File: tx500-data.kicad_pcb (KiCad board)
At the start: 2 copper layers, 50 x 79 mm, 51 parts, among them J1 USB_B_Micro, J2 CAT, J3 REM/DATA, J4 USB_A, U1 TUSB2036, U2 FT232RL, U3 HS-100B, U4 TPS76333, U5 TPS2044D, U6 SN75240, U7 SN75240, Y1 6MHz

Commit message: Add 3D models, and various cleanup
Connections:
- J1 pad 4: (no net) -> Net-(J1-Pad4)
- U1 pad 21: (no net) -> Net-(U1-Pad21)
- U1 pad 32: (no net) -> Net-(U1-Pad32)
- U1 pad 4: (no net) -> Net-(U1-Pad4)
- U1 pad 5: (no net) -> Net-(U1-Pad5)
- U2 pad 10: (no net) -> Net-(U2-Pad10)
- U2 pad 11: (no net) -> Net-(U2-Pad11)
- U2 pad 12: (no net) -> Net-(U2-Pad12)
- U2 pad 13: (no net) -> Net-(U2-Pad13)
- U2 pad 19: (no net) -> Net-(U2-Pad19)
- U2 pad 2: (no net) -> Net-(U2-Pad2)
- U2 pad 22: (no net) -> Net-(U2-Pad22)
- U2 pad 23: (no net) -> Net-(U2-Pad23)
- U2 pad 27: (no net) -> Net-(U2-Pad27)
- U2 pad 28: (no net) -> Net-(U2-Pad28)
- U2 pad 3: (no net) -> Net-(U2-Pad3)
- U2 pad 6: (no net) -> Net-(U2-Pad6)
- U2 pad 9: (no net) -> Net-(U2-Pad9)
- U3 pad 1: (no net) -> Net-(U3-Pad1)
- U3 pad 11: (no net) -> Net-(U3-Pad11)
- U3 pad 17: (no net) -> Net-(U3-Pad17)
- U3 pad 19: (no net) -> Net-(U3-Pad19)
- U3 pad 2: (no net) -> Net-(U3-Pad2)
- U3 pad 26: (no net) -> Net-(U3-Pad26)
- U3 pad 27: (no net) -> Net-(U3-Pad27)
- U3 pad 3: (no net) -> Net-(U3-Pad3)
- U3 pad 31: (no net) -> Net-(U3-Pad31)
- U3 pad 39: (no net) -> Net-(U3-Pad39)
- U3 pad 4: (no net) -> Net-(U3-Pad4)
- U3 pad 41: (no net) -> Net-(U3-Pad41)
- U3 pad 42: (no net) -> Net-(U3-Pad42)
- U3 pad 47: (no net) -> Net-(U3-Pad47)
- U3 pad 5: (no net) -> Net-(U3-Pad5)
- U3 pad 7: (no net) -> Net-(U3-Pad7)
- U4 pad 4: (no net) -> Net-(U4-Pad4)
- U5 pad 10: (no net) -> Net-(U5-Pad10)
- U5 pad 9: (no net) -> Net-(U5-Pad9)
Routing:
- net GNDREF: track 155.4 -> 175.9 mm
- net +3V3: track 57.7 -> 58.6 mm

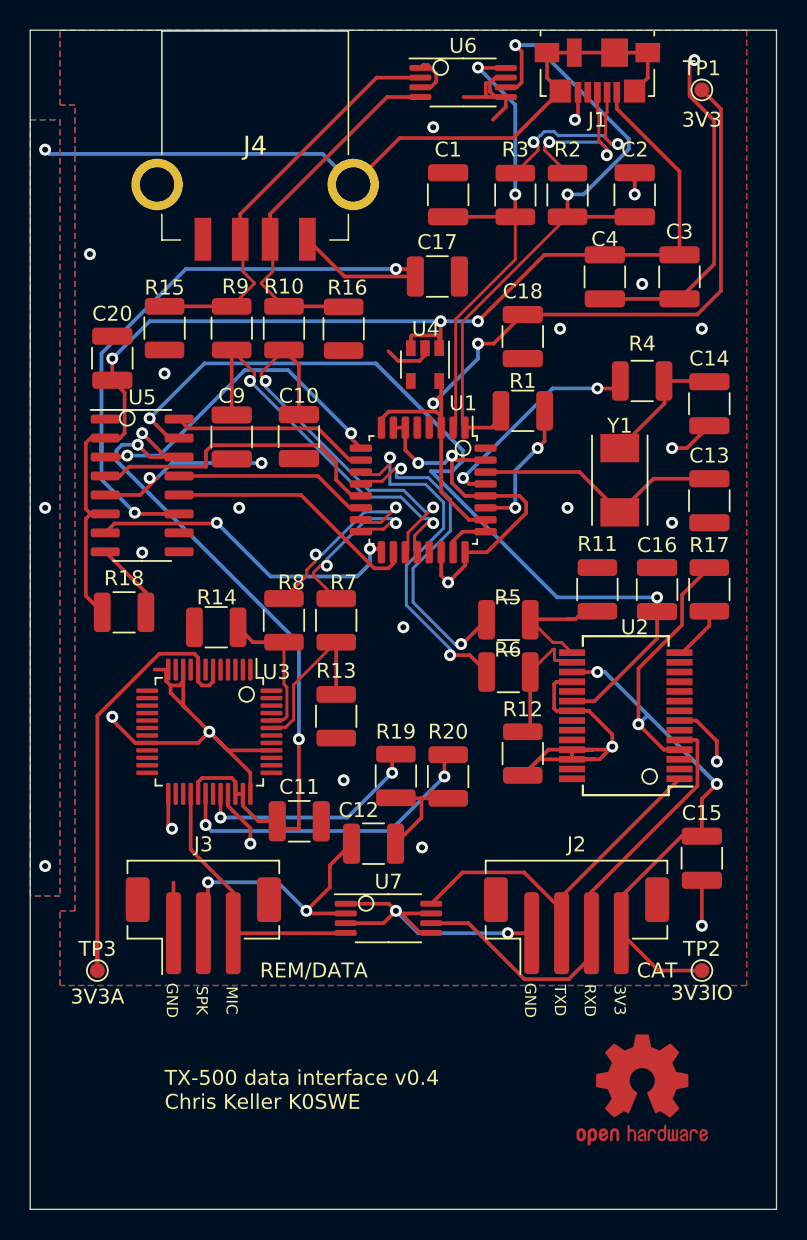
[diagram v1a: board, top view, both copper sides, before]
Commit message: Fix crystal BOM and footprint
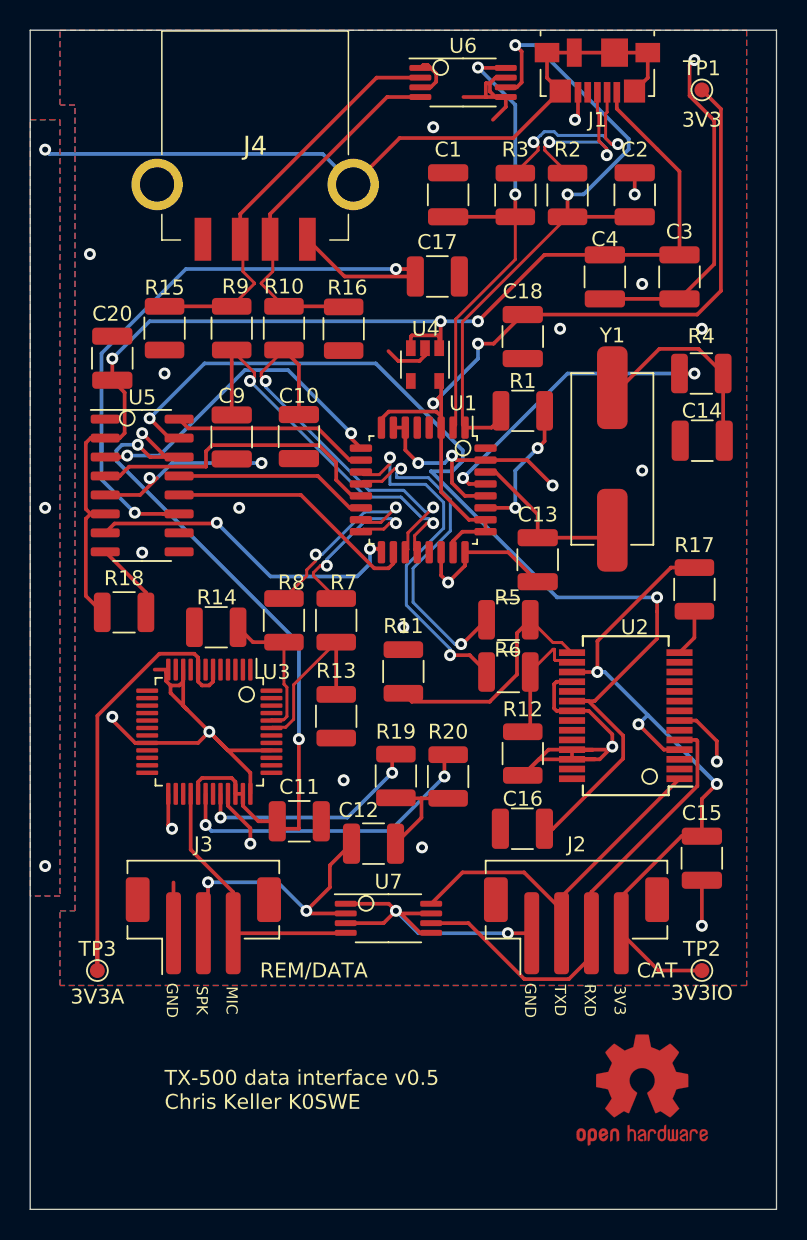
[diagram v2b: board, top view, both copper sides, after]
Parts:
- Y1: footprint Crystal:Crystal_SMD_Abracon_ABM7-2Pin_6.0x3.5mm -> XT49M:XT49M
- moved C16 18.4 mm to (162.0, 111.5), turned to 180 degrees
- moved R11 14.1 mm to (154.0, 101.0)
- moved C13 12.2 mm to (163.0, 93.5)
- moved R4 3.99 mm to (174.0, 81.0)
- moved C14 2.52 mm to (174.0, 85.5), turned to 180 degrees
- moved Y1 1.51 mm to (168.0, 86.7)
- moved R17 1.00 mm to (173.5, 95.5)
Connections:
- J1 pad 4: Net-(J1-Pad4) -> (no net)
- U1 pad 21: Net-(U1-Pad21) -> (no net)
- U1 pad 32: Net-(U1-Pad32) -> (no net)
- U1 pad 4: Net-(U1-Pad4) -> (no net)
- U1 pad 5: Net-(U1-Pad5) -> (no net)
- U2 pad 10: Net-(U2-Pad10) -> (no net)
- U2 pad 11: Net-(U2-Pad11) -> (no net)
- U2 pad 12: Net-(U2-Pad12) -> (no net)
- U2 pad 13: Net-(U2-Pad13) -> (no net)
- U2 pad 19: Net-(U2-Pad19) -> (no net)
- U2 pad 2: Net-(U2-Pad2) -> (no net)
- U2 pad 22: Net-(U2-Pad22) -> (no net)
- U2 pad 23: Net-(U2-Pad23) -> (no net)
- U2 pad 27: Net-(U2-Pad27) -> (no net)
- U2 pad 28: Net-(U2-Pad28) -> (no net)
- U2 pad 3: Net-(U2-Pad3) -> (no net)
- U2 pad 6: Net-(U2-Pad6) -> (no net)
- U2 pad 9: Net-(U2-Pad9) -> (no net)
- U3 pad 1: Net-(U3-Pad1) -> (no net)
- U3 pad 11: Net-(U3-Pad11) -> (no net)
- U3 pad 17: Net-(U3-Pad17) -> (no net)
- U3 pad 19: Net-(U3-Pad19) -> (no net)
- U3 pad 2: Net-(U3-Pad2) -> (no net)
- U3 pad 26: Net-(U3-Pad26) -> (no net)
- U3 pad 27: Net-(U3-Pad27) -> (no net)
- U3 pad 3: Net-(U3-Pad3) -> (no net)
- U3 pad 31: Net-(U3-Pad31) -> (no net)
- U3 pad 39: Net-(U3-Pad39) -> (no net)
- U3 pad 4: Net-(U3-Pad4) -> (no net)
- U3 pad 41: Net-(U3-Pad41) -> (no net)
- U3 pad 42: Net-(U3-Pad42) -> (no net)
- U3 pad 47: Net-(U3-Pad47) -> (no net)
- U3 pad 5: Net-(U3-Pad5) -> (no net)
- U3 pad 7: Net-(U3-Pad7) -> (no net)
- U4 pad 4: Net-(U4-Pad4) -> (no net)
- U5 pad 10: Net-(U5-Pad10) -> (no net)
- U5 pad 9: Net-(U5-Pad9) -> (no net)
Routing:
- net /5VA: track 59.4 -> 72.5 mm
- net Net-(R11-Pad1): track 8.88 -> 16.3 mm
- net Net-(C14-Pad1): track 7.69 -> 13.9 mm
- net /XTAL2: track 14.9 -> 21.1 mm
- net /XTAL1: track 17.0 -> 11.4 mm
- net /3V3IO: track 53.0 -> 51.2 mm
- net GNDREF: track 175.9 -> 174.9 mm, vias 31 -> 30
- net /PWREN: track 3.72 -> 3.19 mm
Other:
- board text added: "TX-500 data interface v0.5 Chris Keller K0SWE"
- board text removed: "TX-500 data interface v0.4 Chris Keller K0SWE"

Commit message: Use standard footprint for crystal
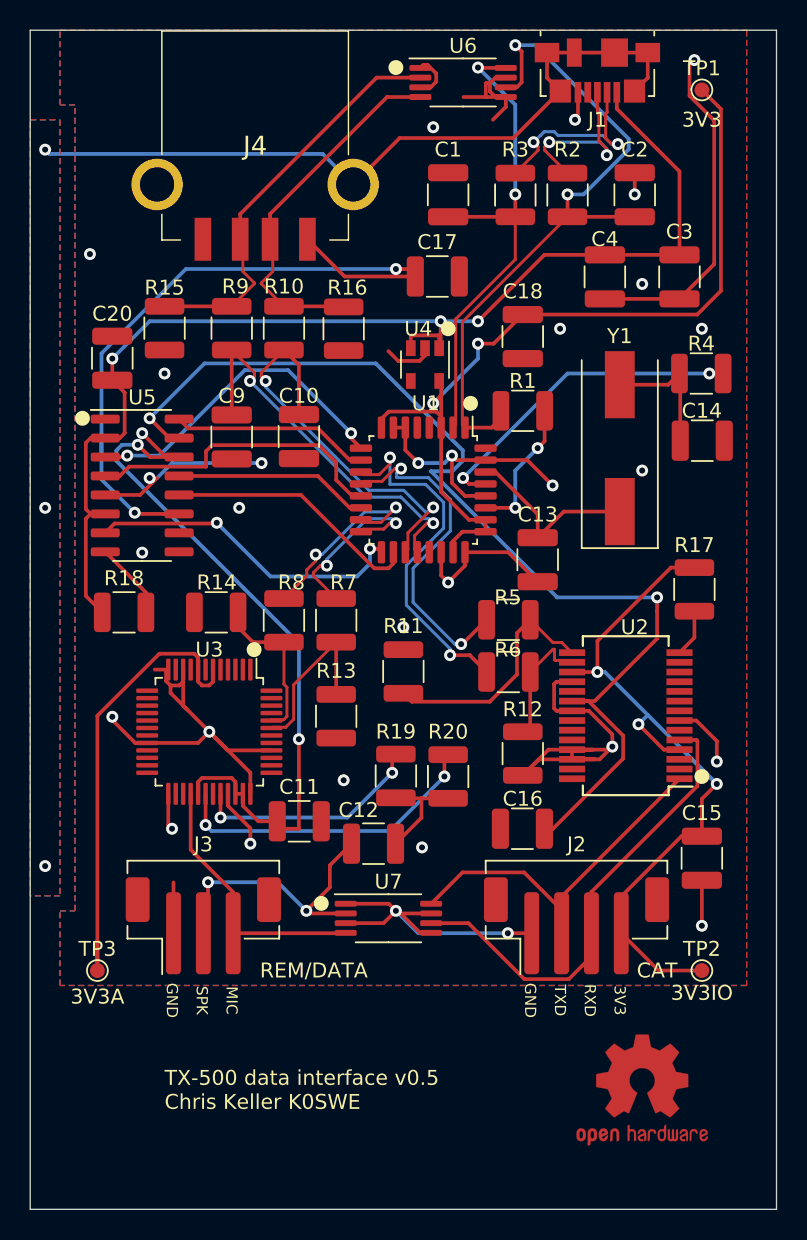
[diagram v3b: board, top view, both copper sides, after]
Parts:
- Y1: footprint XT49M:XT49M -> Crystal:Crystal_SMD_HC49-SD
- moved R14 1.00 mm to (141.5, 97.0)
- moved Y1 0.88 mm to (168.5, 86.0)
- turned C14 to 0 degrees
- turned R4 to 0 degrees
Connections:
- J1 pad 4: (no net) -> Net-(J1-Pad4)
- U1 pad 21: (no net) -> Net-(U1-Pad21)
- U1 pad 32: (no net) -> Net-(U1-Pad32)
- U1 pad 4: (no net) -> Net-(U1-Pad4)
- U1 pad 5: (no net) -> Net-(U1-Pad5)
- U2 pad 10: (no net) -> Net-(U2-Pad10)
- U2 pad 11: (no net) -> Net-(U2-Pad11)
- U2 pad 12: (no net) -> Net-(U2-Pad12)
- U2 pad 13: (no net) -> Net-(U2-Pad13)
- U2 pad 19: (no net) -> Net-(U2-Pad19)
- U2 pad 2: (no net) -> Net-(U2-Pad2)
- U2 pad 22: (no net) -> Net-(U2-Pad22)
- U2 pad 23: (no net) -> Net-(U2-Pad23)
- U2 pad 27: (no net) -> Net-(U2-Pad27)
- U2 pad 28: (no net) -> Net-(U2-Pad28)
- U2 pad 3: (no net) -> Net-(U2-Pad3)
- U2 pad 6: (no net) -> Net-(U2-Pad6)
- U2 pad 9: (no net) -> Net-(U2-Pad9)
- U3 pad 1: (no net) -> Net-(U3-Pad1)
- U3 pad 11: (no net) -> Net-(U3-Pad11)
- U3 pad 17: (no net) -> Net-(U3-Pad17)
- U3 pad 19: (no net) -> Net-(U3-Pad19)
- U3 pad 2: (no net) -> Net-(U3-Pad2)
- U3 pad 26: (no net) -> Net-(U3-Pad26)
- U3 pad 27: (no net) -> Net-(U3-Pad27)
- U3 pad 3: (no net) -> Net-(U3-Pad3)
- U3 pad 31: (no net) -> Net-(U3-Pad31)
- U3 pad 39: (no net) -> Net-(U3-Pad39)
- U3 pad 4: (no net) -> Net-(U3-Pad4)
- U3 pad 41: (no net) -> Net-(U3-Pad41)
- U3 pad 42: (no net) -> Net-(U3-Pad42)
- U3 pad 47: (no net) -> Net-(U3-Pad47)
- U3 pad 5: (no net) -> Net-(U3-Pad5)
- U3 pad 7: (no net) -> Net-(U3-Pad7)
- U4 pad 4: (no net) -> Net-(U4-Pad4)
- U5 pad 10: (no net) -> Net-(U5-Pad10)
- U5 pad 9: (no net) -> Net-(U5-Pad9)
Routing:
- net Net-(C14-Pad1): track 13.9 -> 8.19 mm
- net /XTAL1: track 11.4 -> 13.1 mm
- net /XTAL2: track 21.1 -> 22.0 mm
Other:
- board text added: "https://github.com/k0swe/tx500-data-interface"

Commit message: Use smaller dimensions capacitor
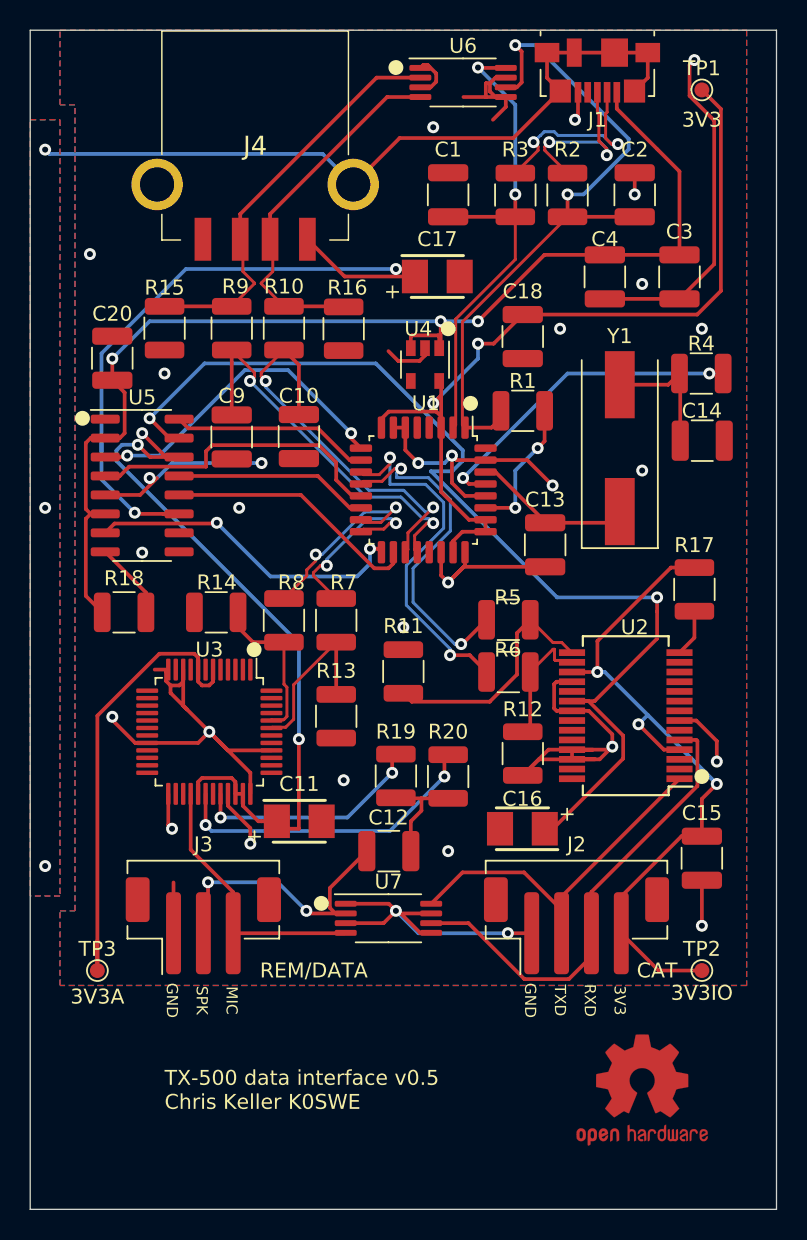
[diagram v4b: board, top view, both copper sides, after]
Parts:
- C11, C16, C17: footprint Capacitor_SMD:C_1210_3225Metric -> 6TPE120MAZB:CAPPM3528X200N
- moved C12 1.14 mm to (153.0, 113.0)
- moved C13 1.12 mm to (163.5, 92.5)
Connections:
- J1 pad 4: Net-(J1-Pad4) -> (no net)
- U1 pad 21: Net-(U1-Pad21) -> (no net)
- U1 pad 32: Net-(U1-Pad32) -> (no net)
- U1 pad 4: Net-(U1-Pad4) -> (no net)
- U1 pad 5: Net-(U1-Pad5) -> (no net)
- U2 pad 10: Net-(U2-Pad10) -> (no net)
- U2 pad 11: Net-(U2-Pad11) -> (no net)
- U2 pad 12: Net-(U2-Pad12) -> (no net)
- U2 pad 13: Net-(U2-Pad13) -> (no net)
- U2 pad 19: Net-(U2-Pad19) -> (no net)
- U2 pad 2: Net-(U2-Pad2) -> (no net)
- U2 pad 22: Net-(U2-Pad22) -> (no net)
- U2 pad 23: Net-(U2-Pad23) -> (no net)
- U2 pad 27: Net-(U2-Pad27) -> (no net)
- U2 pad 28: Net-(U2-Pad28) -> (no net)
- U2 pad 3: Net-(U2-Pad3) -> (no net)
- U2 pad 6: Net-(U2-Pad6) -> (no net)
- U2 pad 9: Net-(U2-Pad9) -> (no net)
- U3 pad 1: Net-(U3-Pad1) -> (no net)
- U3 pad 11: Net-(U3-Pad11) -> (no net)
- U3 pad 17: Net-(U3-Pad17) -> (no net)
- U3 pad 19: Net-(U3-Pad19) -> (no net)
- U3 pad 2: Net-(U3-Pad2) -> (no net)
- U3 pad 26: Net-(U3-Pad26) -> (no net)
- U3 pad 27: Net-(U3-Pad27) -> (no net)
- U3 pad 3: Net-(U3-Pad3) -> (no net)
- U3 pad 31: Net-(U3-Pad31) -> (no net)
- U3 pad 39: Net-(U3-Pad39) -> (no net)
- U3 pad 4: Net-(U3-Pad4) -> (no net)
- U3 pad 41: Net-(U3-Pad41) -> (no net)
- U3 pad 42: Net-(U3-Pad42) -> (no net)
- U3 pad 47: Net-(U3-Pad47) -> (no net)
- U3 pad 5: Net-(U3-Pad5) -> (no net)
- U3 pad 7: Net-(U3-Pad7) -> (no net)
- U4 pad 4: Net-(U4-Pad4) -> (no net)
- U5 pad 10: Net-(U5-Pad10) -> (no net)
- U5 pad 9: Net-(U5-Pad9) -> (no net)
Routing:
- net /XTAL1: track 13.1 -> 11.4 mm
- net GNDREF: track 175.0 -> 176.2 mm

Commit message: Thicker 5V traces and clean up case grounds
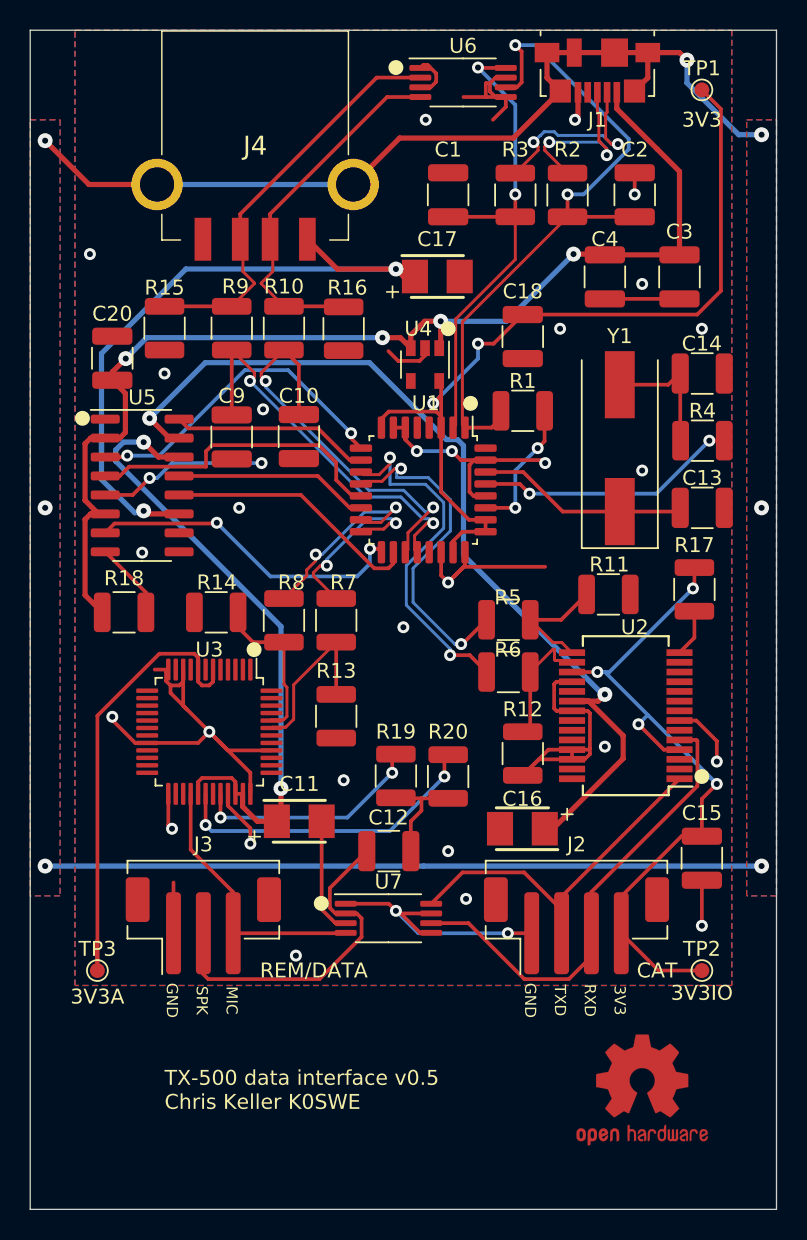
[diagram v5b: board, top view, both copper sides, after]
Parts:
- moved R11 14.7 mm to (167.7, 95.8), turned to 0 degrees
- moved C13 10.8 mm to (174.0, 90.0), turned to 0 degrees
- moved R4 4.50 mm to (174.0, 85.5)
- moved C14 4.50 mm to (174.0, 81.0)
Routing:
- net GND1: track 50.7 -> 109.8 mm, vias 3 -> 7
- net GNDREF: track 176.2 -> 154.0 mm, vias 30 -> 32
- net /5VA: track 72.5 -> 63.6 mm
- net Net-(R11-Pad1): track 16.3 -> 8.19 mm
- net /5VB: track 48.3 -> 42.8 mm, vias 3 -> 2
- net /XTAL2: track 22.0 -> 17.7 mm
- net /SPK: track 19.7 -> 23.1 mm, vias 2 -> 0
- net /XTAL1: track 11.4 -> 14.9 mm
- net VBUS: track 79.8 -> 77.7 mm, vias 3 -> 4
- net /5VC: track 48.6 -> 47.6 mm
- net /3V3IO: track 51.2 -> 50.7 mm, vias 3 -> 4
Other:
- net class Power added: clearance 0.2, trace_width 0.35, via_dia 1, via_drill 0.4
- rule trace_min: 0.2 -> 0.16

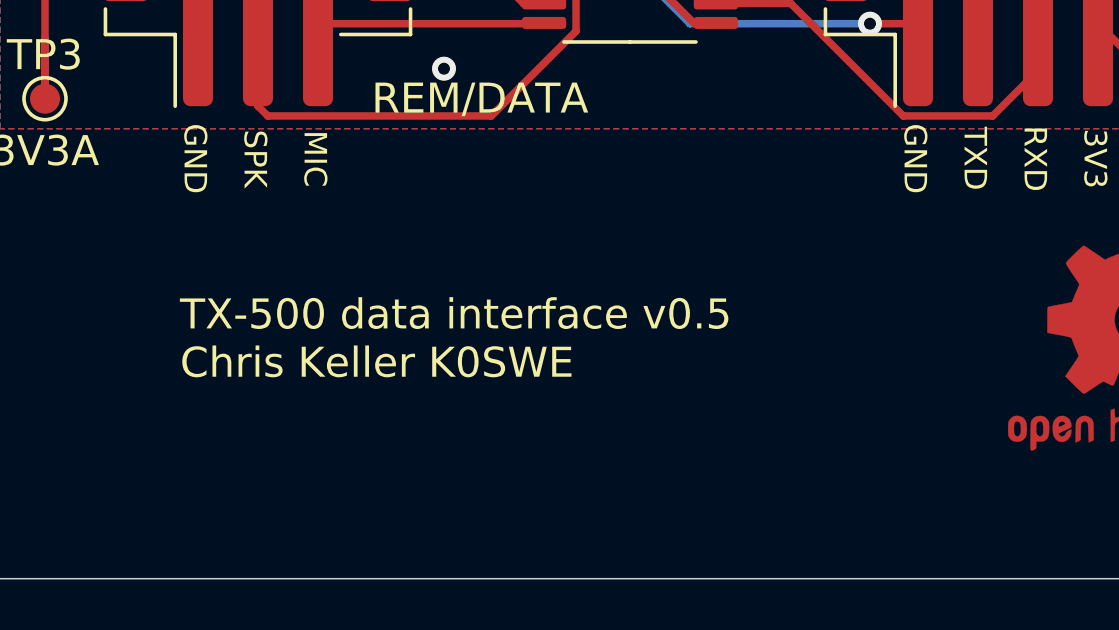
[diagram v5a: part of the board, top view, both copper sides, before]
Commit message: Change license to CC-BY-4.0
CC is more conducive to open hardware than Apache
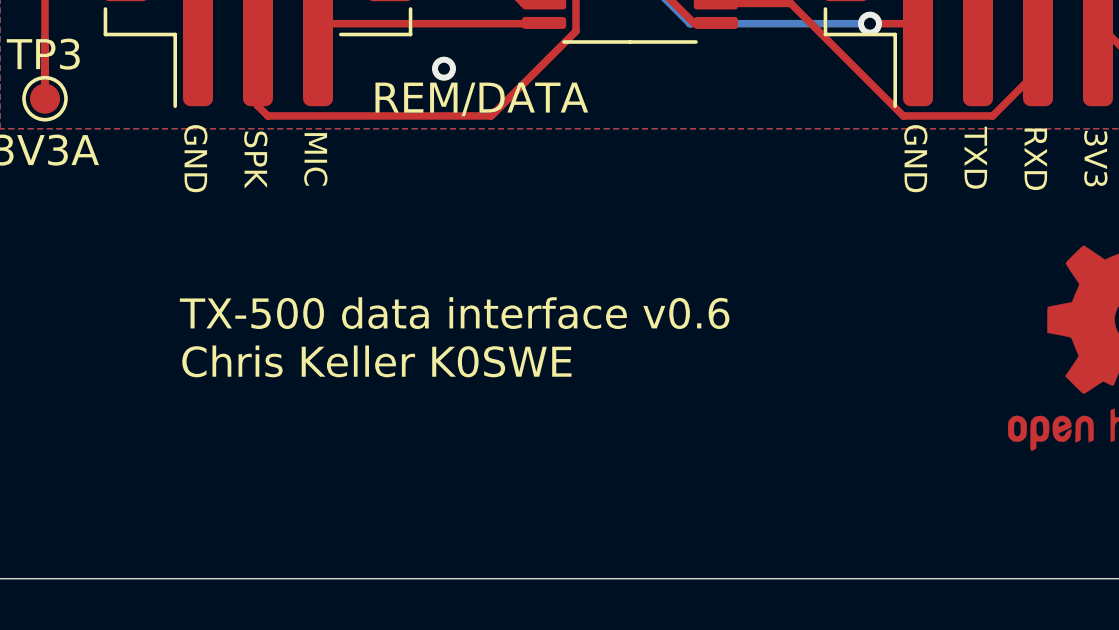
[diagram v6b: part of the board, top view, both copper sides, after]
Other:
- board text added: "TX-500 data interface v0.6 Chris Keller K0SWE"
- board text removed: "TX-500 data interface v0.5 Chris Keller K0SWE"
